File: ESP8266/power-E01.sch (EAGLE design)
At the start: 11 parts, among them CON1 USBMICRO-NO_CENTER

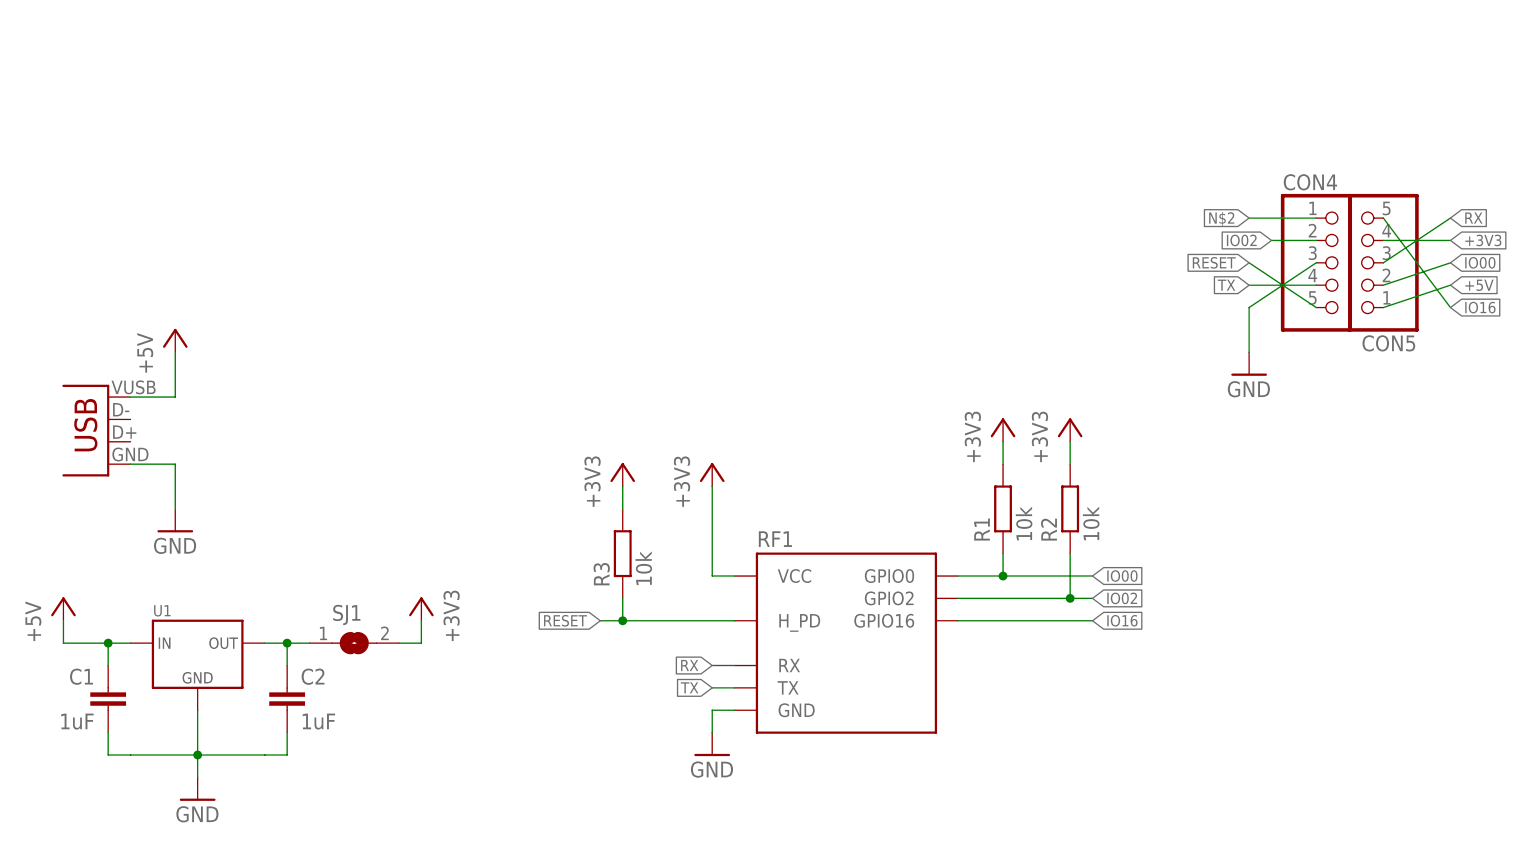
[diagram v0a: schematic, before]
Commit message: Added some adapters for ESP8266 01 module
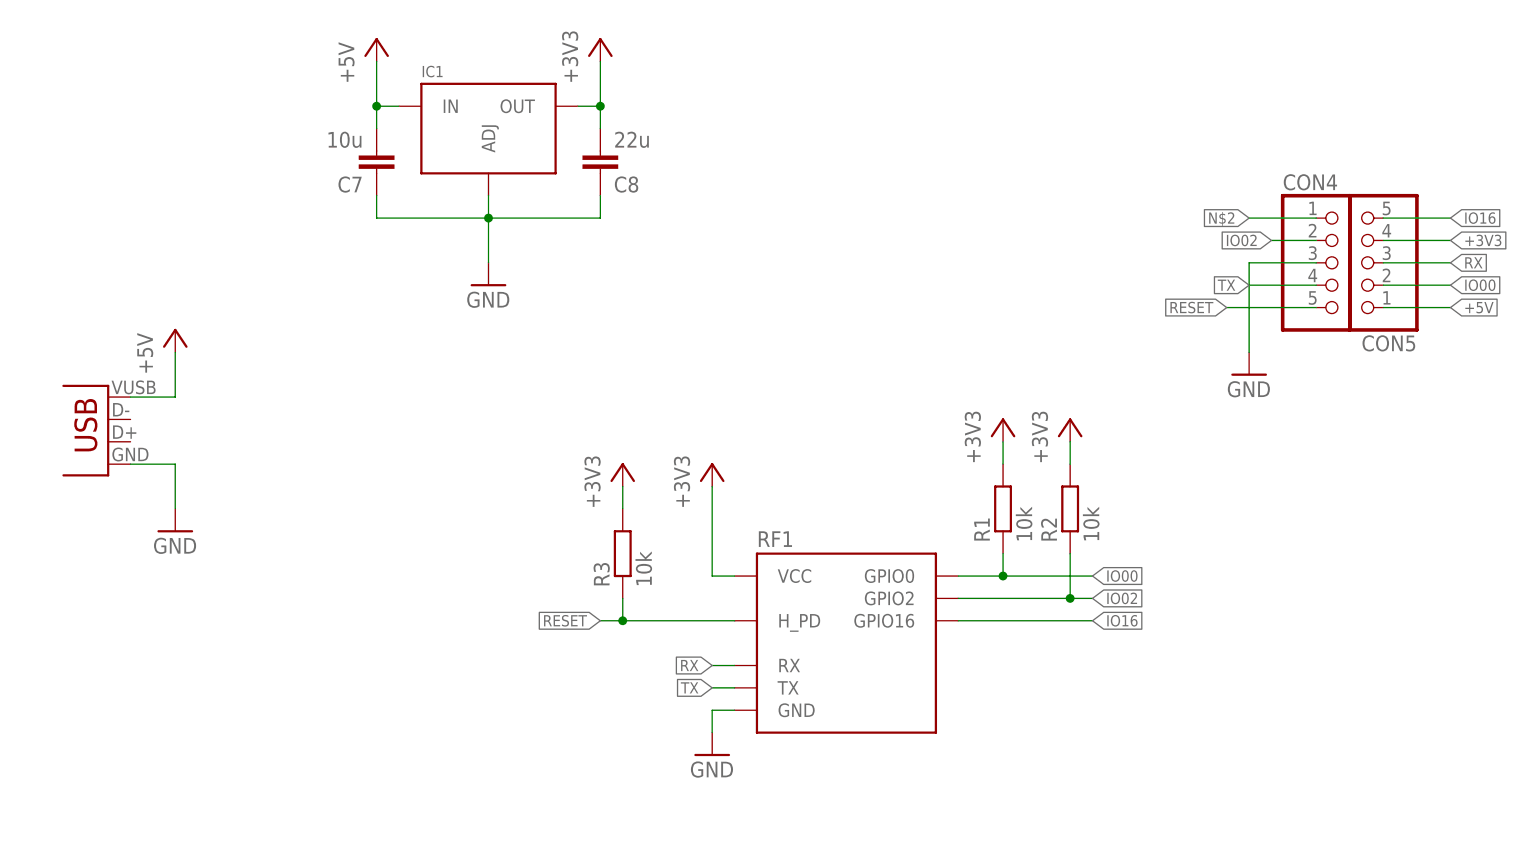
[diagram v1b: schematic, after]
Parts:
- removed C1, C2: 1uF, p.peter-rcl:C-EUC0805
- removed SJ1: (no value), jumper:SJ
- removed U1: (no value), p.peter-regulators:REGULATOR-XC6206SOT23
- added C7: 10u, p.peter-rcl:C-EUC0805
- added C8: 22u, p.peter-rcl:C-EUC0805
- added IC1: (no value), p.peter-regulators:REGULATOR-LM317-SOT223
- RF1: device p.peter-periphery:ESP2866-ESP-01THT -> p.peter-periphery:ESP2866-ESP-01THT-NOSILK
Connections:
- removed net N$1: C2.1, SJ1.1, U1.OUT
- net +3V3: now also C8.2, IC1.OUT; no longer SJ1.2
- net +5V: now also C7.2, IC1.IN; no longer C1.1, U1.IN
- net GND: now also C7.1, C8.1, IC1.ADJ; no longer C1.2, C2.2, U1.GND
